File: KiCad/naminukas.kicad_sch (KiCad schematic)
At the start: 0 parts

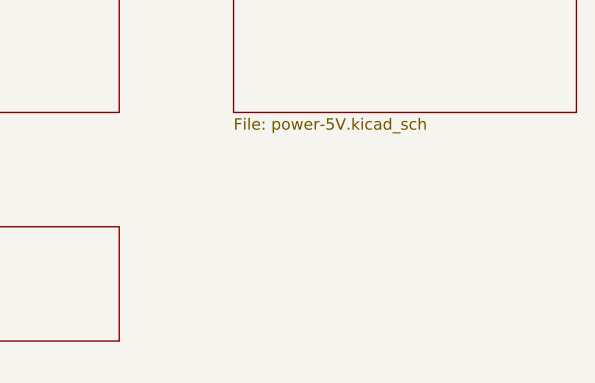
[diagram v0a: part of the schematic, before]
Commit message: feat(pcb): add schematic for battery
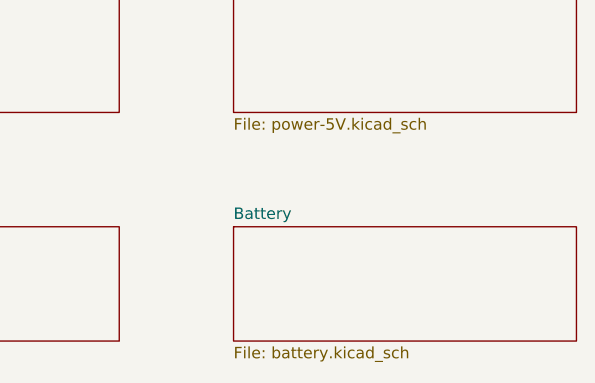
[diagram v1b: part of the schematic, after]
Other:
- added sheet Battery (battery.kicad_sch)
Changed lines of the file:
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@@
+    )
+  )
+  (sheet (at 177.8 50.8) (size 38.1 12.7) (fields_autoplaced)
+    (stroke (width 0.1524) (type solid) (color 0 0 0 0))
+    (fill (color 0 0 0 0.0000))
+    (property "Sheet name" "Battery" (id 0) (at 177.8 50.0884 0)
+      (effects (font (size 1.27 1.27)) (justify left bottom))
+    )
+    (property "Sheet file" "battery.kicad_sch" (id 1) (at 177.8 64.0846 0)
+      (effects (font (size 1.27 1.27)) (justify left top))
     )
   )
@@
     (path "/7089617d-8d3f-4f47-8b6f-cc7f9c0fdff0" (page "7"))
     (path "/077fc97f-933b-4652-8be7-bc0954415a95" (page "8"))
+    (path "/7741455d-c4a2-42e1-804a-9627c39f590b" (page "9"))
   )
   (symbol_instances
+    (path "/7741455d-c4a2-42e1-804a-9627c39f590b/3a218306-fc16-400b-9606-5b146a901f71"
+      (reference "#FLG0101") (unit 1) (value "PWR_FLAG") (footprint "")
+    )
+    (path "/7741455d-c4a2-42e1-804a-9627c39f590b/37bda2f7-a66a-43e0-9118-ba2e26f31f34"
+      (reference "#FLG0102") (unit 1) (value "PWR_FLAG") (footprint "")
+    )
+    (path "/7741455d-c4a2-42e1-804a-9627c39f590b/358deb86-c51d-42cc-8d8e-306683f5f020"
+      (reference "#PWR0101") (unit 1) (value "GND") (footprint "")
+    )
+    (path "/7741455d-c4a2-42e1-804a-9627c39f590b/a52f25f4-d906-4e7a-984f-aff0550fa9fc"
+      (reference "#PWR0102") (unit 1) (value "+BATT") (footprint "")
+    )
+    (path "/077fc97f-933b-4652-8be7-bc0954415a95/13ae8a5c-8a12-40e1-9b5c-c52be1ded986"
+      (reference "#PWR0103") (unit 1) (value "GND") (footprint "")
+    )
+    (path "/7741455d-c4a2-42e1-804a-9627c39f590b/f329dd40-ccdd-431c-8ac3-2f169afe676f"
+      (reference "BT1") (unit 1) (value "Battery") (footprint "")
+    )
     (path "/077fc97f-933b-4652-8be7-bc0954415a95/f2ed8b26-4361-4d72-ae94-4e46a6affc6f"
-      (reference "U?") (unit 1) (value "TPSM63606RDLR") (footprint "RDL0020A-MFG")
+      (reference "U1") (unit 1) (value "TPSM63606RDLR") (footprint "RDL0020A-MFG")
     )
   )
